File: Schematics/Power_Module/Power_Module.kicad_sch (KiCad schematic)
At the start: 34 parts, among them J1 2-1445057-2, J2 2-1445057-2, J3 2-1445057-2, J5 2-1445057-2, J6 Stack Male Edge Connector, Q1 AO4485, Q2 AO4485, U1 LMR51430XDDCR, U2 LMR51430XDDCR, U3 LMR51430XDDCR

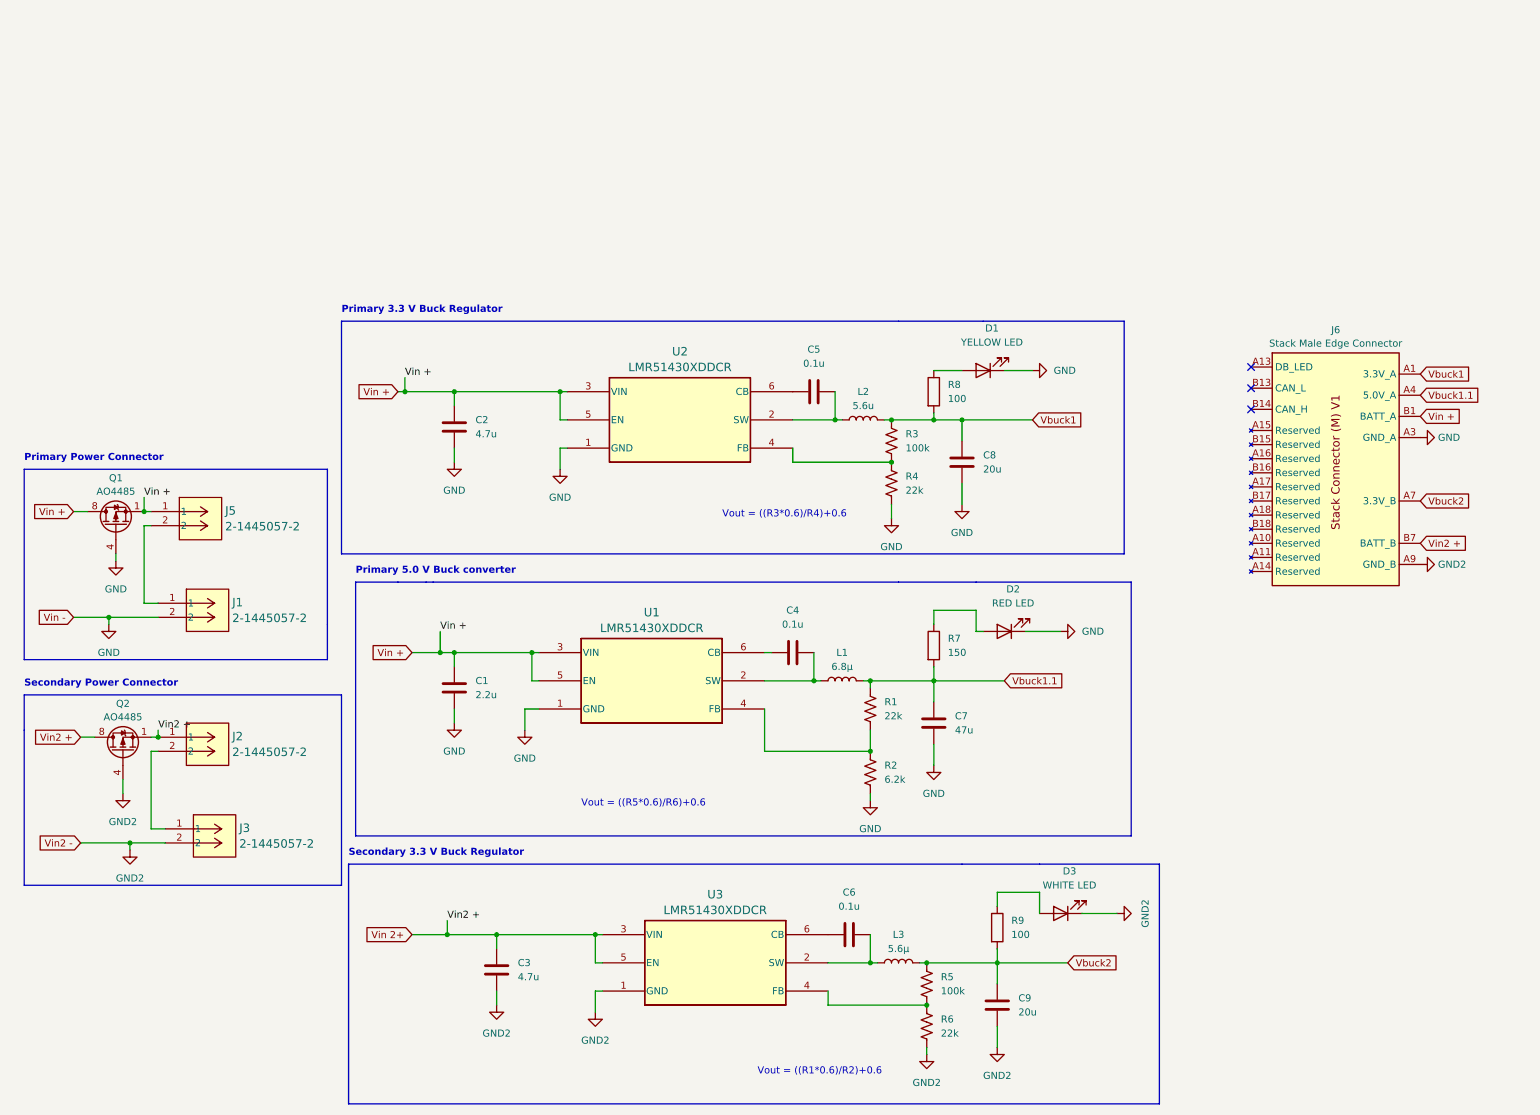
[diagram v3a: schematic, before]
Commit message: Reorganized schematic, added attribution, adjusted parts
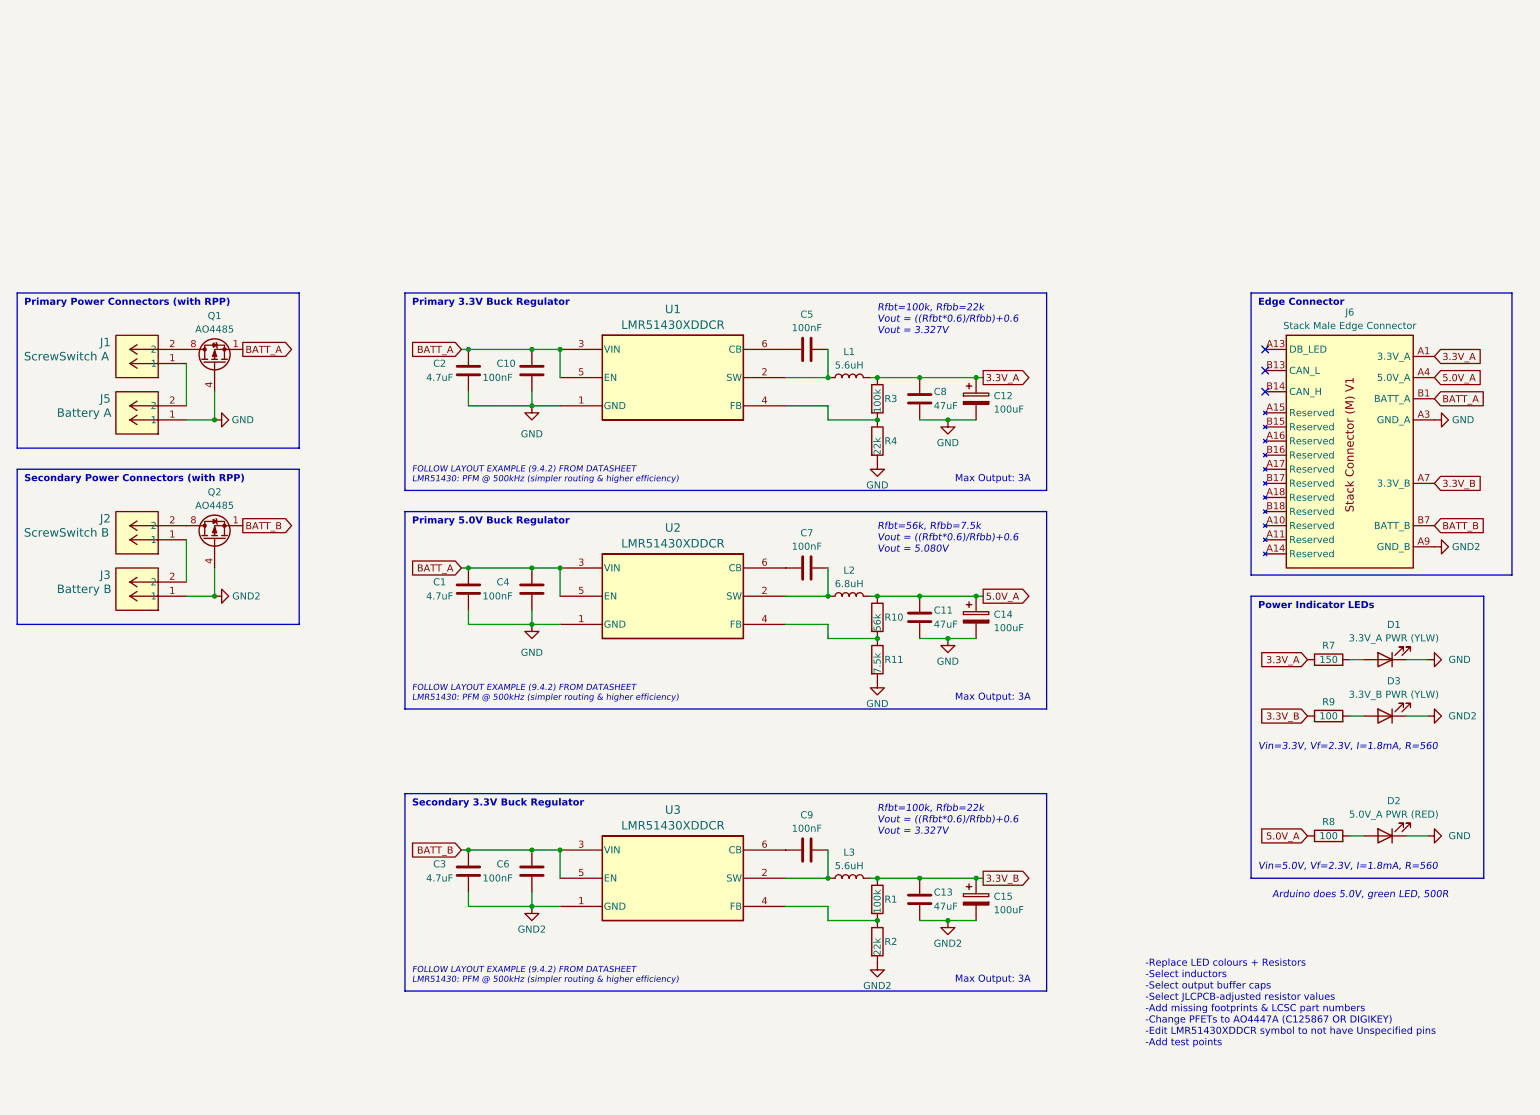
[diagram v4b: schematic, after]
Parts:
- removed R1, R4, R6: 22k, Resistor_SMD:R_0603_1608Metric, symbol Device:R_US
- removed R2: 6.2k, Resistor_SMD:R_0603_1608Metric, symbol Device:R_US
- removed R3, R5: 100k, Resistor_SMD:R_0603_1608Metric, symbol Device:R_US
- removed U1: LMR51430XDDCR, Package_TO_SOT_SMD:SOT-23-6_Handsoldering, symbol QRET_Buck_PSU-symbols:LMR51430XDDCR
- added C10: 100nF, Capacitor_SMD:C_0603_1608Metric, symbol Device:C
- added C11, C13: 47uF, Capacitor_SMD:C_0603_1608Metric, symbol Device:C
- added C12, C14, C15: 100uF, Capacitor_SMD:CP_Elec_4x5.4, symbol Device:C_Polarized
- added R1, R3: 100k, symbol Device:R
- added R10: 56k, symbol Device:R
- added R11: 7.5k, symbol Device:R
- added R2, R4: 22k, symbol Device:R
- added U2: LMR51430XDDCR, Package_TO_SOT_SMD:SOT-23-6_Handsoldering, symbol QRET_Buck_PSU-symbols:LMR51430XDDCR
- C1: value 2.2u -> 4.7uF; LCSC C76612 -> (none)
- C2, C3: value 4.7u -> 4.7uF; LCSC C71631 -> (none)
- C4, C5, C6: value 0.1u -> 100nF; Part # C0603C104M3RAC7867 -> (none)
- C7: value 47u -> 100nF; LCSC C2185054 -> (none)
- C8: value 20u -> 47uF; Part # GRMJN7R61C206ME05D -> (none)
- C9: value 20u -> 100nF; Part # GRMJN7R61C206ME05D -> (none)
- D1: value YELLOW LED -> 3.3V_A PWR (YLW)
- D2: value RED LED -> 5.0V_A PWR (RED)
- D3: value WHITE LED -> 3.3V_B PWR (YLW)
- J1: value 2-1445057-2 -> ScrewSwitch A
- J2: value 2-1445057-2 -> ScrewSwitch B
- J3: value 2-1445057-2 -> Battery B
- J5: value 2-1445057-2 -> Battery A
- L1: renamed from L2; value 5.6u -> 5.6uH; LCSC C5137243 -> (none)
- L2: renamed from L1; value 6.8µ -> 6.8uH; LCSC C5137248 -> (none)
- L3: value 5.6µ -> 5.6uH; LCSC C139205 -> (none)
- renumbered U2 to U1
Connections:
- net 5.0V_A: now also R8.1, C11.1, C14.1, R10.1; no longer C7.1, R7.2
- net GND: now also C4.2, J5.1, C10.2, C11.2, C12.2, C14.2, R11.2, R4.2, U2.1 (GND); no longer C7.2, J1.2
- net GND2: now also C6.2, J3.1, C13.2, C15.2, R2.2; no longer C9.2, J3.2
- net at L3.1, U3.2 (SW): now also C9.1; no longer C6.2
- net at U3.4 (FB): now also R1.2, R2.1
- net at U3.6 (CB): now also C9.2; no longer C6.1
- net at C5.1: now also L1.1, U1.2 (SW); no longer U1.6 (CB)
- net at L2.1: now also C7.1, U2.2 (SW); no longer C4.2
- net BATT_A: now reaches C4.1
- net BATT_A: now also C1.1, C2.1, J6.B1 (BATT_A), J6.B2 (BATT_A), J6.B3 (BATT_A), Q1.1 (S), Q1.2 (S), Q1.3 (S), U1.3 (VIN), U1.5 (EN), C10.1, U2.3 (VIN), U2.5 (EN)
- net at U1.4 (FB): now also R3.2, R4.1
- net at J2.2: now also Q2.5 (D), Q2.6 (D), Q2.7 (D), Q2.8 (D); no longer J3.1
- net at D1.2 (A): now also R7.2; no longer R8.1
- net at D2.2 (A): now also R8.2; no longer R7.1
- net at D3.2 (A): now also R9.2; no longer R9.1
- net Vbuck1 renamed 3.3V_A
- net 3.3V_A: now also R7.1, C12.1, R3.1; no longer R8.2
- net Vbuck2 renamed 3.3V_B
- net 3.3V_B: now also R9.1, C13.1, C15.1, R1.1; no longer C9.1, R9.2
- removed net Vin +: C1.1, C2.1, J5.1, J6.B1 (BATT_A), J6.B2 (BATT_A), J6.B3 (BATT_A), Q1.1 (S), Q1.2 (S), Q1.3 (S), Q1.5 (D), Q1.6 (D), Q1.7 (D), Q1.8 (D), U1.3 (VIN), U1.5 (EN)
- net Vin 2+ renamed BATT_B
- net BATT_B: now also C6.1; no longer J2.1, Q2.5 (D), Q2.6 (D), Q2.7 (D), Q2.8 (D)
- new net: C5.2, U1.6 (CB)
- new net: R10.2, R11.1, U2.4 (FB)
- new net: C7.2, U2.6 (CB)
- new net: J1.2, Q1.5 (D), Q1.6 (D), Q1.7 (D), Q1.8 (D)
- new net: J2.1, J3.2
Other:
- note added: "-Replace LED colours + Resistors -Select inductors -Select output buffer caps -Select JLCPCB-adjusted resistor values -Add missing footprints & LCSC part numbers -Change PFETs to AO4447A (C125867 OR DIGIKEY) -Edit LMR51430XDDCR symbol to not have Unspecified pins -Add test points"
- note added: "Arduino does 5.0V, green LED, 500R"
- note added: "Edge Connector"
- note added: "FOLLOW LAYOUT EXAMPLE (9.4.2) FROM DATASHEET LMR51430: PFM @ 500kHz (simpler routing & higher efficiency)"
- note added: "Max Output: 3A"
- note added: "Power Indicator LEDs"
- note added: "Primary 3.3V Buck Regulator"
- note added: "Primary 5.0V Buck Regulator"
- note added: "Primary Power Connectors (with RPP)"
- note added: "Rfbt=100k, Rfbb=22k Vout = ((Rfbt*0.6)/Rfbb)+0.6 Vout = 3.327V"
- note added: "Rfbt=56k, Rfbb=7.5k Vout = ((Rfbt*0.6)/Rfbb)+0.6 Vout = 5.080V"
- note added: "Secondary 3.3V Buck Regulator"
- note added: "Secondary Power Connectors (with RPP)"
- note added: "Vin=3.3V, Vf=2.3V, I=1.8mA, R=560"
- note added: "Vin=5.0V, Vf=2.3V, I=1.8mA, R=560"
- note removed: "Primary 3.3 V Buck Regulator"
- note removed: "Primary 5.0 V Buck converter"
- note removed: "Primary Power Connector"
- note removed: "Secondary 3.3 V Buck Regulator"
- note removed: "Secondary Power Connector"
- note removed: "Vout = ((R1*0.6)/R2)+0.6"
- note removed: "Vout = ((R3*0.6)/R4)+0.6"
- note removed: "Vout = ((R5*0.6)/R6)+0.6"
- company: (none) -> Queen's Rocket Engineering Team
- moved on the sheet: C2, C5, D1, D2, D3, J1, J5, J6, L1, L2, Q1, R7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

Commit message: Selected inductors & capacitors
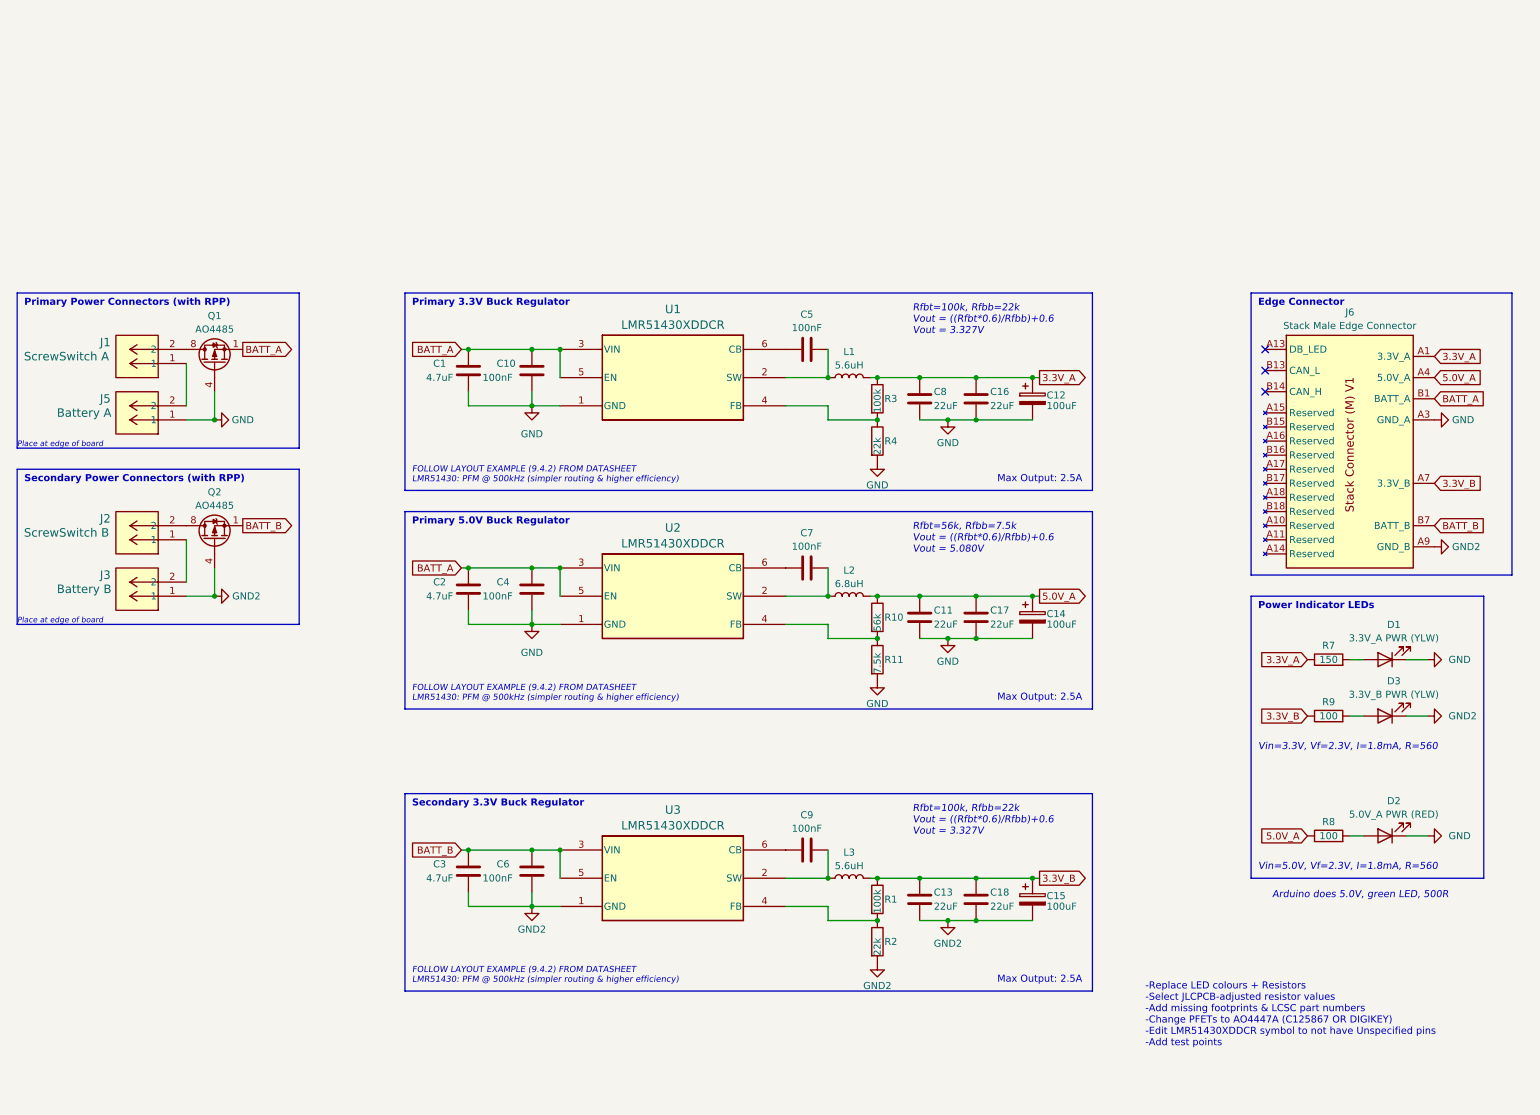
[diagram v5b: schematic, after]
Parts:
- added C16, C17, C18: 22uF, Capacitor_SMD:C_0805_2012Metric, symbol Device:C
- C1, C2, C3: footprint Capacitor_SMD:C_0603_1608Metric -> Capacitor_SMD:C_0805_2012Metric; LCSC (none) -> C1779
- C10, C4, C5, C6, C7, C9: LCSC (none) -> C14663
- C11, C13, C8: value 47uF -> 22uF; footprint Capacitor_SMD:C_0603_1608Metric -> Capacitor_SMD:C_0805_2012Metric; LCSC (none) -> C45783
- C12, C14, C15: footprint Capacitor_SMD:CP_Elec_4x5.4 -> Capacitor_SMD:CP_Elec_6.3x5.9; Digikey (none) -> 732-8419-1-ND
- L1, L3: footprint (none) -> Inductor_SMD:L_Bourns_SRN8040TA; Digikey (none) -> SDCHA1V8040-5R6-R
- L2: footprint (none) -> Inductor_SMD:L_Bourns_SRN8040TA; Digikey (none) -> HPC 8040NC-6R8M
- R1, R3: footprint (none) -> Resistor_SMD:R_0603_1608Metric; LCSC (none) -> C25803
- R10: footprint (none) -> Resistor_SMD:R_0603_1608Metric; LCSC (none) -> C23206
- R11: footprint (none) -> Resistor_SMD:R_0603_1608Metric; LCSC (none) -> C23234
- R2, R4: footprint (none) -> Resistor_SMD:R_0603_1608Metric; LCSC (none) -> C31850
- R7: LCSC C22808 -> (none)
- R8, R9: LCSC C22775 -> (none)
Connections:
- net 3.3V_A: now also C16.1
- net 3.3V_B: now also C18.1
- net 5.0V_A: now also C17.1
- net GND: now also C16.2, C17.2
- net GND2: now also C18.2
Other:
- note added: "-Replace LED colours + Resistors -Select JLCPCB-adjusted resistor values -Add missing footprints & LCSC part numbers -Change PFETs to AO4447A (C125867 OR DIGIKEY) -Edit LMR51430XDDCR symbol to not have Unspecified pins -Add test points"
- note added: "Max Output: 2.5A"
- note added: "Place at edge of board"
- note removed: "-Replace LED colours + Resistors -Select inductors -Select output buffer caps -Select JLCPCB-adjusted resistor values -Add missing footprints & LCSC part numbers -Change PFETs to AO4447A (C125867 OR DIGIKEY) -Edit LMR51430XDDCR symbol to not have Unspecified pins -Add test points"
- note removed: "Max Output: 3A"

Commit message: Updated LMR51430 footprint
Shrunk it slightly and changed any "Unspecified" pins to "Passive"
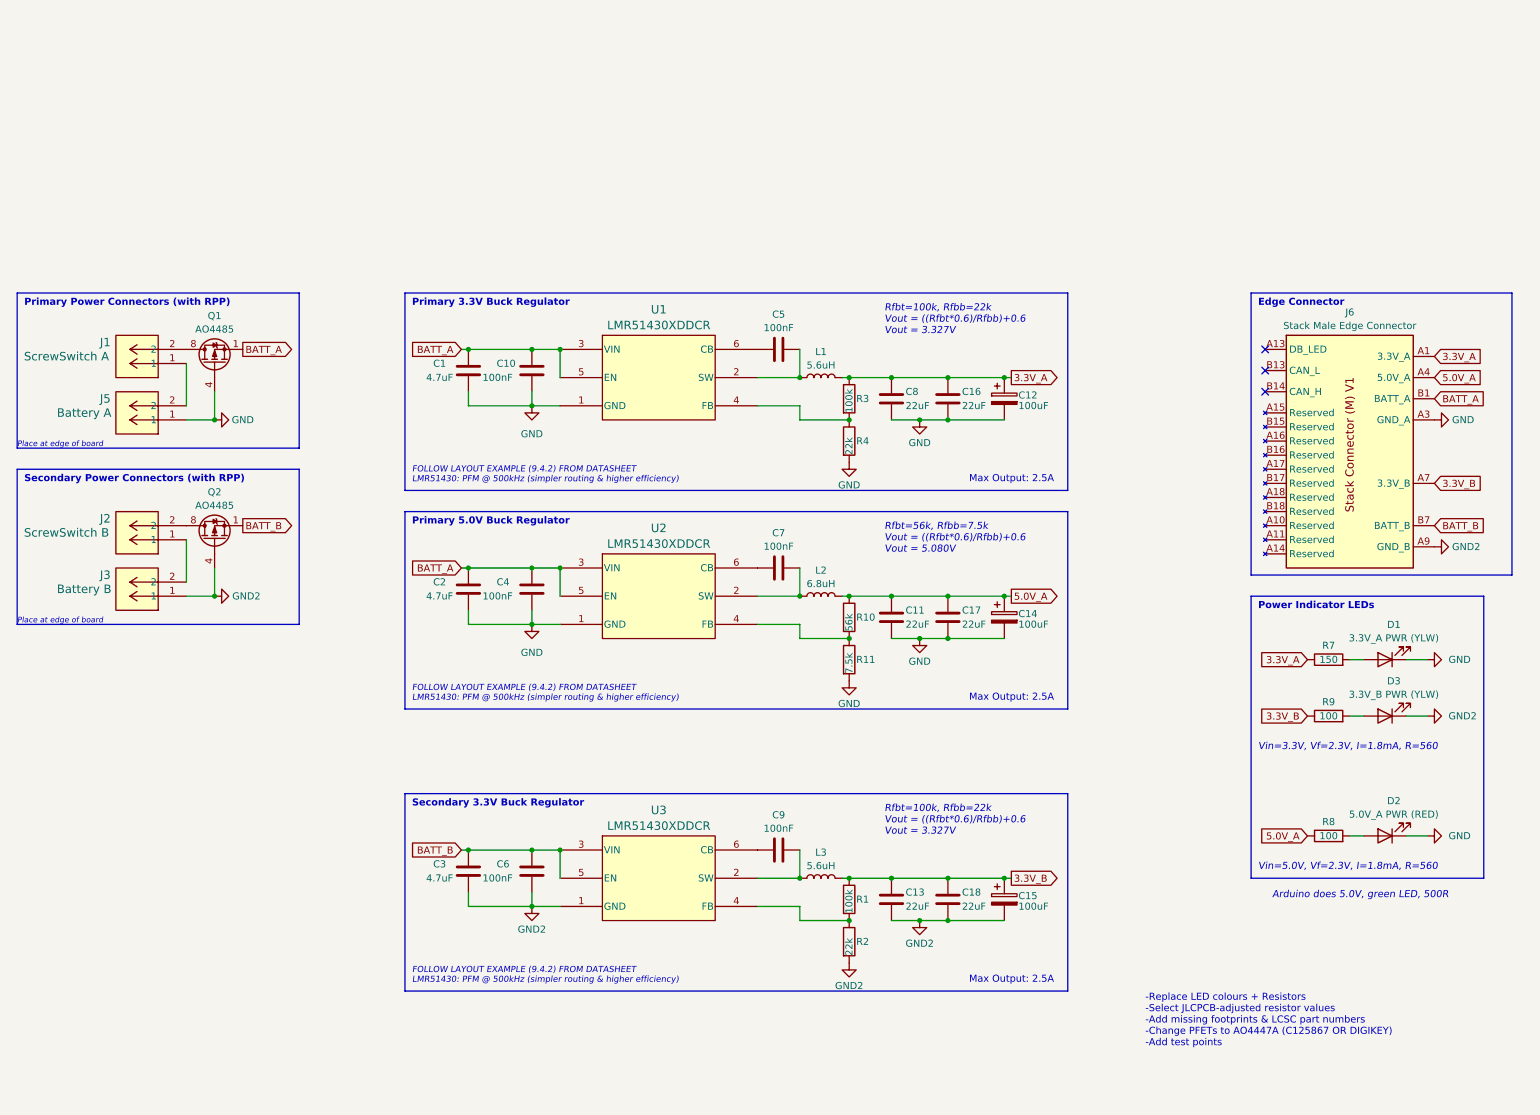
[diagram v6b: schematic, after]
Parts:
- U1, U2, U3: Digikey (none) -> 296-LMR51430XDDCRCT-ND
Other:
- note added: "-Replace LED colours + Resistors -Select JLCPCB-adjusted resistor values -Add missing footprints & LCSC part numbers -Change PFETs to AO4447A (C125867 OR DIGIKEY) -Add test points"
- note removed: "-Replace LED colours + Resistors -Select JLCPCB-adjusted resistor values -Add missing footprints & LCSC part numbers -Change PFETs to AO4447A (C125867 OR DIGIKEY) -Edit LMR51430XDDCR symbol to not have Unspecified pins -Add test points"
- moved on the sheet: C11, C12, C13, C14, C15, C16, C17, C18, C5, C7, C8, C9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
